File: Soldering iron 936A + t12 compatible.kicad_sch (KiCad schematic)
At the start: 109 parts, among them J1 DC INPUT, J2 USB TO SERIAL, J3 AC input, J4 output_connector, J5 mosfet_driver_future_backup, J6 OLED, J7 USB C BREAKOUT BOARD, Q1 IRF9540N, Q2 BC547, SW1 RotaryEncoder_Switch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

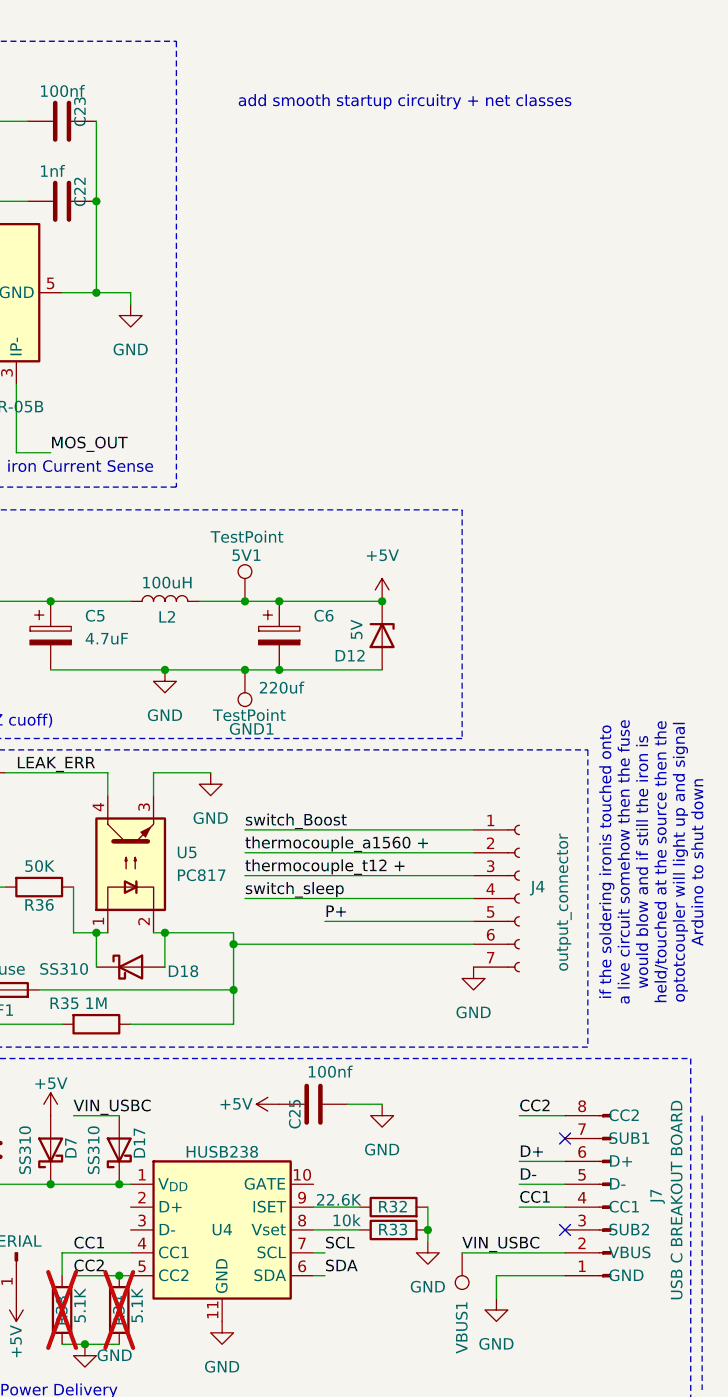
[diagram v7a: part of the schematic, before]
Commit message: Layout fully complete yet to be reviewed
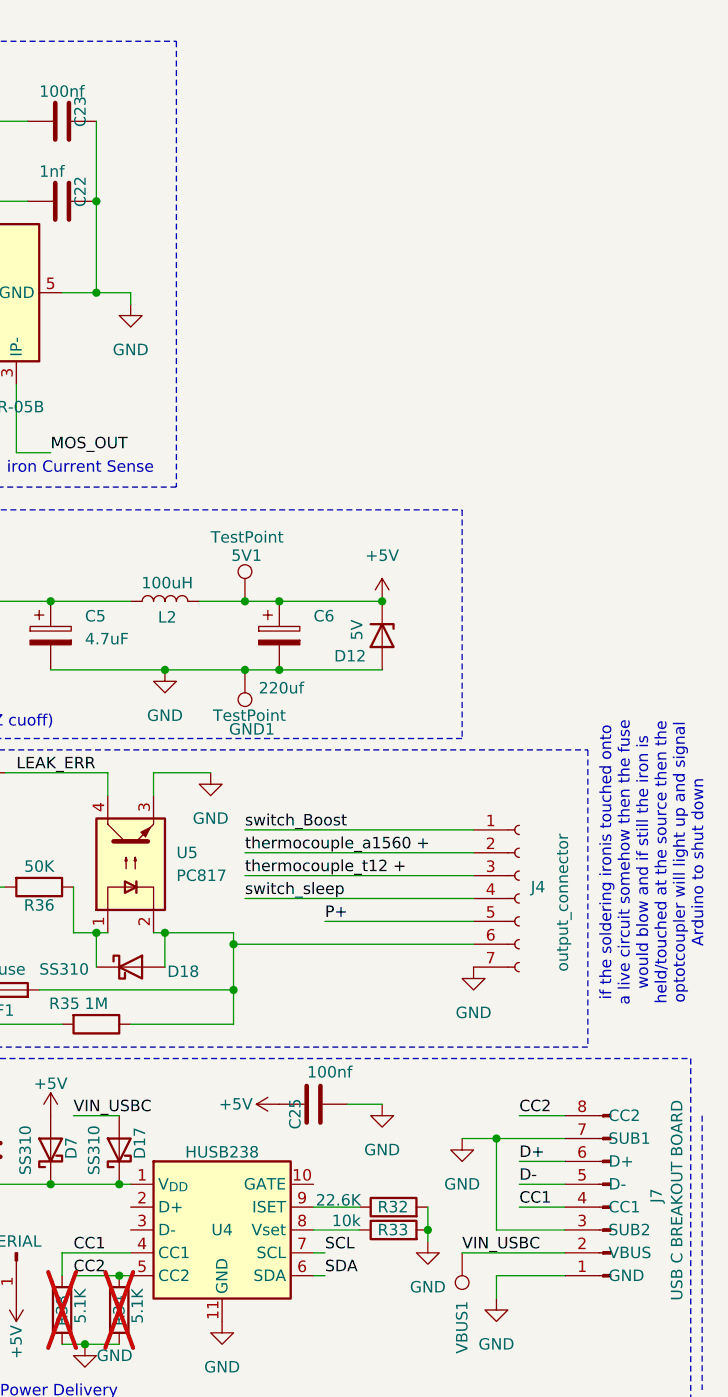
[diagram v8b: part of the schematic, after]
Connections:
- net GND: now also J7.3 (SUB2), J7.7 (SUB1)
- no-connect marks 4 -> 2
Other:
- note removed: "add smooth startup circuitry + net classes"
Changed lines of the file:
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@@
 		)
 	)
-	(text "add smooth startup circuitry + net classes\n"
-		(exclude_from_sim no)
-		(at 251.46 22.098 0)
-		(effects
-			(font
-				(size 1.27 1.27)
-			)
-		)
-	)
 	(text "MAIN BRAINS"
 		(exclude_from_sim no)
@@
 	)
 	(junction
+		(at 261.62 137.16)
+		(diameter 0)
+		(color 0 0 0 0)
+	)
+	(junction
 		(at 215.9 160.02)
 		(diameter 0)
@@
 	)
 	(no_connect
-		(at 269.24 147.32)
-	)
-	(no_connect
 		(at 74.93 19.05)
 	)
-	(no_connect
-		(at 269.24 137.16)
-	)
 	(wire
 		(pts
@@
 	(wire
 		(pts
+			(xy 261.62 147.32) (xy 261.62 137.16)
+		)
+		(stroke
+			(width 0)
+			(type default)
+		)
+	)
+	(wire
+		(pts
 			(xy 151.13 72.39) (xy 151.13 73.66)
 		)
@@
 	(wire
 		(pts
+			(xy 257.81 137.16) (xy 261.62 137.16)
+		)
+		(stroke
+			(width 0)
+			(type default)
+		)
+	)
+	(wire
+		(pts
 			(xy 62.23 161.29) (xy 63.5 161.29)
 		)
@@
 	(wire
 		(pts
+			(xy 261.62 137.16) (xy 269.24 137.16)
+		)
+		(stroke
+			(width 0)
+			(type default)
+		)
+	)
+	(wire
+		(pts
 			(xy 140.97 53.34) (xy 161.29 53.34)
 		)
@@
 	(wire
 		(pts
+			(xy 269.24 147.32) (xy 261.62 147.32)
+		)
+		(stroke
+			(width 0)
+			(type default)
+		)
+	)
+	(wire
+		(pts
 			(xy 59.69 59.69) (xy 64.77 59.69)
 		)
@@
 					(unit 1)
 				)
+			)
+		)
+	)
+	(symbol
+		(lib_id "power:GND")
+		(at 257.81 137.16 0)
+		(mirror y)
+		(unit 1)
+		(exclude_from_sim no)
+		(in_bom yes)
+		(on_board yes)
+		(dnp no)
+		(property "Reference" "#PWR057"
+			(at 257.81 143.51 0)
+			(effects
+				(font
+					(size 1.27 1.27)
+				)
+				(hide yes)
+			)
+		)
+		(property "Value" "GND"
+			(at 257.81 142.24 0)
+			(effects
+				(font
+					(size 1.27 1.27)
+				)
+			)
+		)
+		(property "Footprint" ""
+			(at 257.81 137.16 0)
+			(effects
+				(font
+					(size 1.27 1.27)
+				)
+				(hide yes)
+			)
+		)
+		(property "Datasheet" ""
+			(at 257.81 137.16 0)
+			(effects
+				(font
+					(size 1.27 1.27)
+				)
+				(hide yes)
+			)
+		)
+		(property "Description" "Power symbol creates a global label with name \"GND\" , ground"
+			(at 257.81 137.16 0)
+			(effects
+				(font
+					(size 1.27 1.27)
+				)
+				(hide yes)
+			)
+		)
+		(pin "1"
+		)
+		(instances
+			(project "Soldering iron 936A + t12 compatible"
+				(path "/7b8f23b9-5775-45f1-8dbe-ed5fada41d3e"
+					(reference "#PWR057")
+					(unit 1)
+				)
